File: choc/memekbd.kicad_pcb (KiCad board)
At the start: 2 copper layers, 277.8 x 199.5 mm, 162 parts, among them J1 USB_B_Micro, J2 USB_B_Micro, SW1 SW_Push, SW10 SW_Push, SW11 SW_Push, SW12 SW_Push, SW13 SW_Push, SW14 SW_Push, SW15 SW_Push, SW16 SW_Push, SW17 SW_Push, SW18 SW_Push, SW19 SW_Push, SW2 SW_Push, SW20 SW_Push, SW21 SW_Push, SW22 SW_Push, SW23 SW_Push, SW24 SW_Push, SW25 SW_Push, SW26 SW_Push, SW27 SW_Push, SW28 SW_Push, SW29 SW_Push, SW3 SW_Push, SW30 SW_Push, SW31 SW_Push, SW32 SW_Push, SW33 SW_Push, SW34 SW_Push, SW35 SW_Push, SW36 SW_Push, SW37 SW_Push, SW38 SW_Push, SW39 SW_Push, SW4 SW_Push, SW40 SW_Push, SW41 SW_Push, SW42 SW_Push, SW43 SW_Push, SW44 SW_Push, SW45 SW_Push, SW46 SW_Push, SW47 SW_Push, SW48 SW_Push, SW49 SW_Push, SW5 SW_Push, SW50 SW_Push, SW6 SW_Push, SW7 SW_Push, SW8 SW_Push, SW9 SW_Push, U1 ProMicro, U2 ProMicro

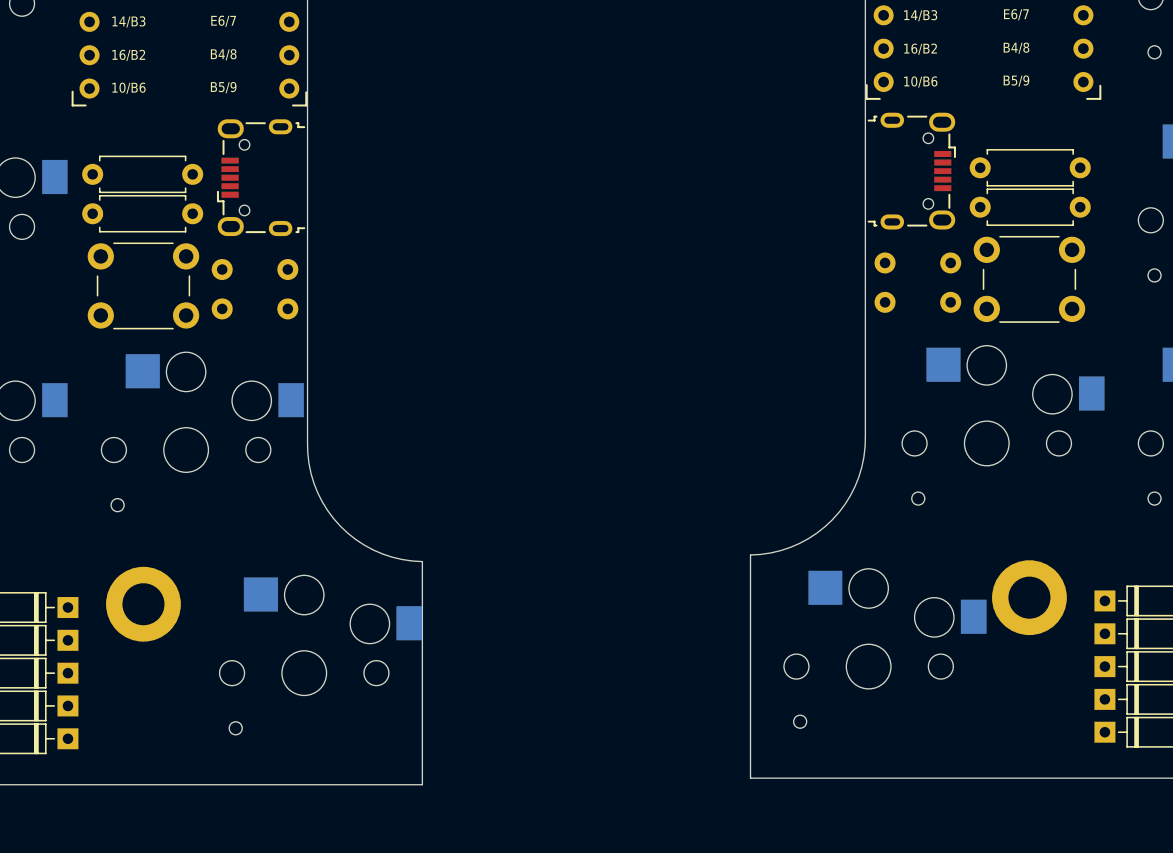
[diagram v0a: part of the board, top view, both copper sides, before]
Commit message: add buzzer to pcb
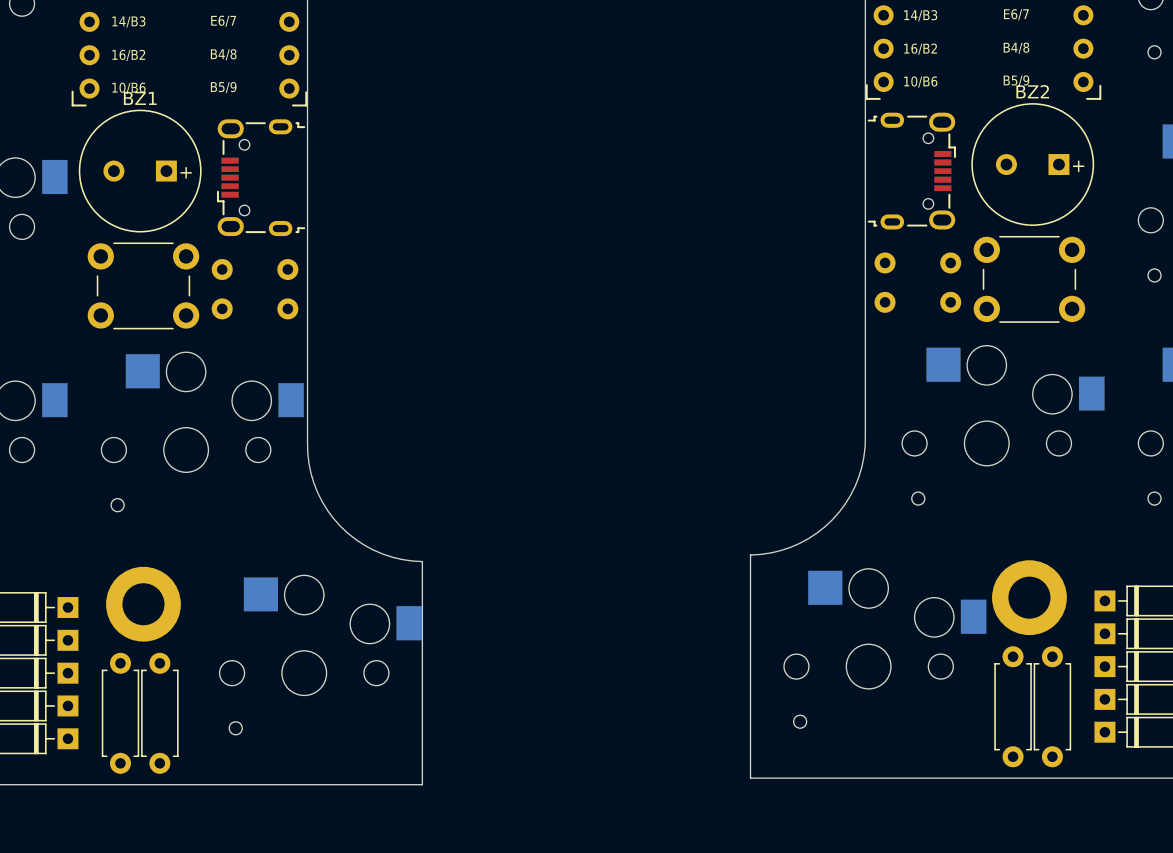
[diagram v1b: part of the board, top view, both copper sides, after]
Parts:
- added BZ1: Buzzer, Buzzer_Beeper:MagneticBuzzer_PUI_AT-0927-TT-6-R, F.Cu at (113.5, 63.5)
- added BZ2: Buzzer, Buzzer_Beeper:MagneticBuzzer_PUI_AT-0927-TT-6-R, F.Cu at (181.5, 63.0)
- moved R1 37.7 mm to (110.0, 101.0), turned to -90 degrees
- moved R4 37.7 mm to (181.0, 100.5), turned to -90 degrees
- moved R2 34.3 mm to (113.0, 101.0), turned to -90 degrees
- moved R3 34.3 mm to (178.0, 100.5), turned to -90 degrees
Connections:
- U1 pad 12: unconnected-(U1-Pad12) -> /lbuzzer
- U2 pad 12: unconnected-(U2-Pad12) -> /rbuzzer

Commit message: update location of resistors. fix bug in top plate
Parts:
- moved R2 46.0 mm to (68.0, 91.2), turned to 180 degrees
- moved R3 46.0 mm to (223.0, 90.8), turned to 0 degrees
- moved R1 43.9 mm to (68.0, 88.2), turned to 180 degrees
- moved R4 43.9 mm to (223.0, 87.8), turned to 0 degrees
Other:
- outline, holes or cut-outs redrawn
